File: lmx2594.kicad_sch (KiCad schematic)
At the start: 46 parts, among them J32 TUNESENSE, U21 LMX2594

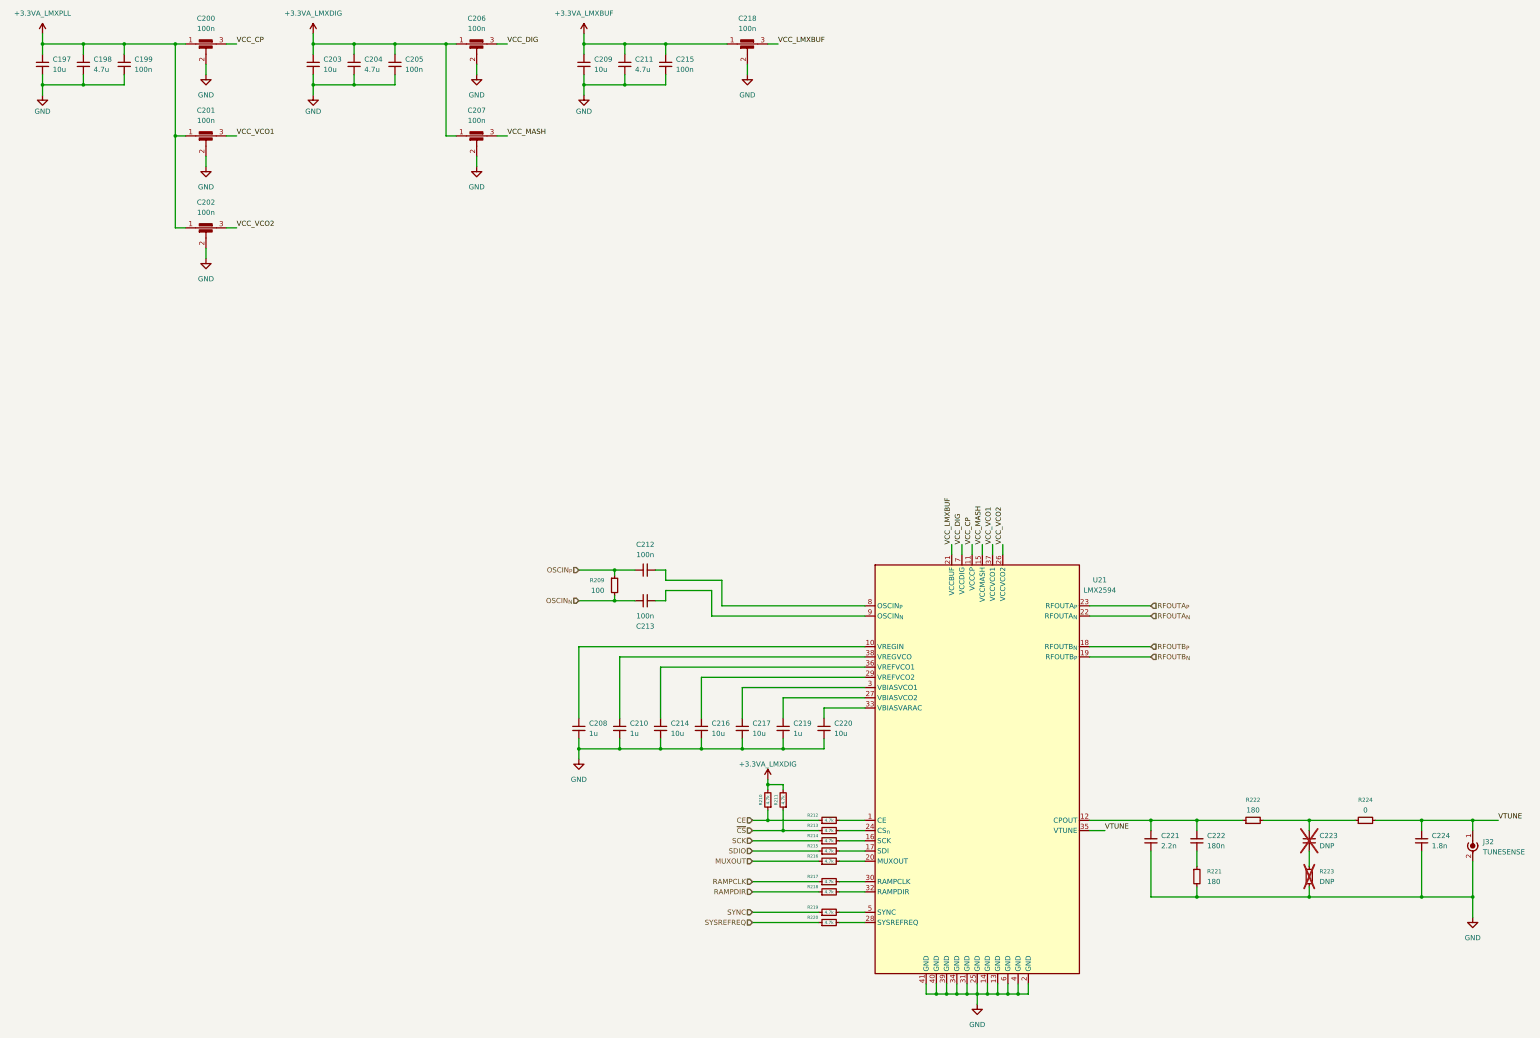
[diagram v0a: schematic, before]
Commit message: Different Matching Circuit
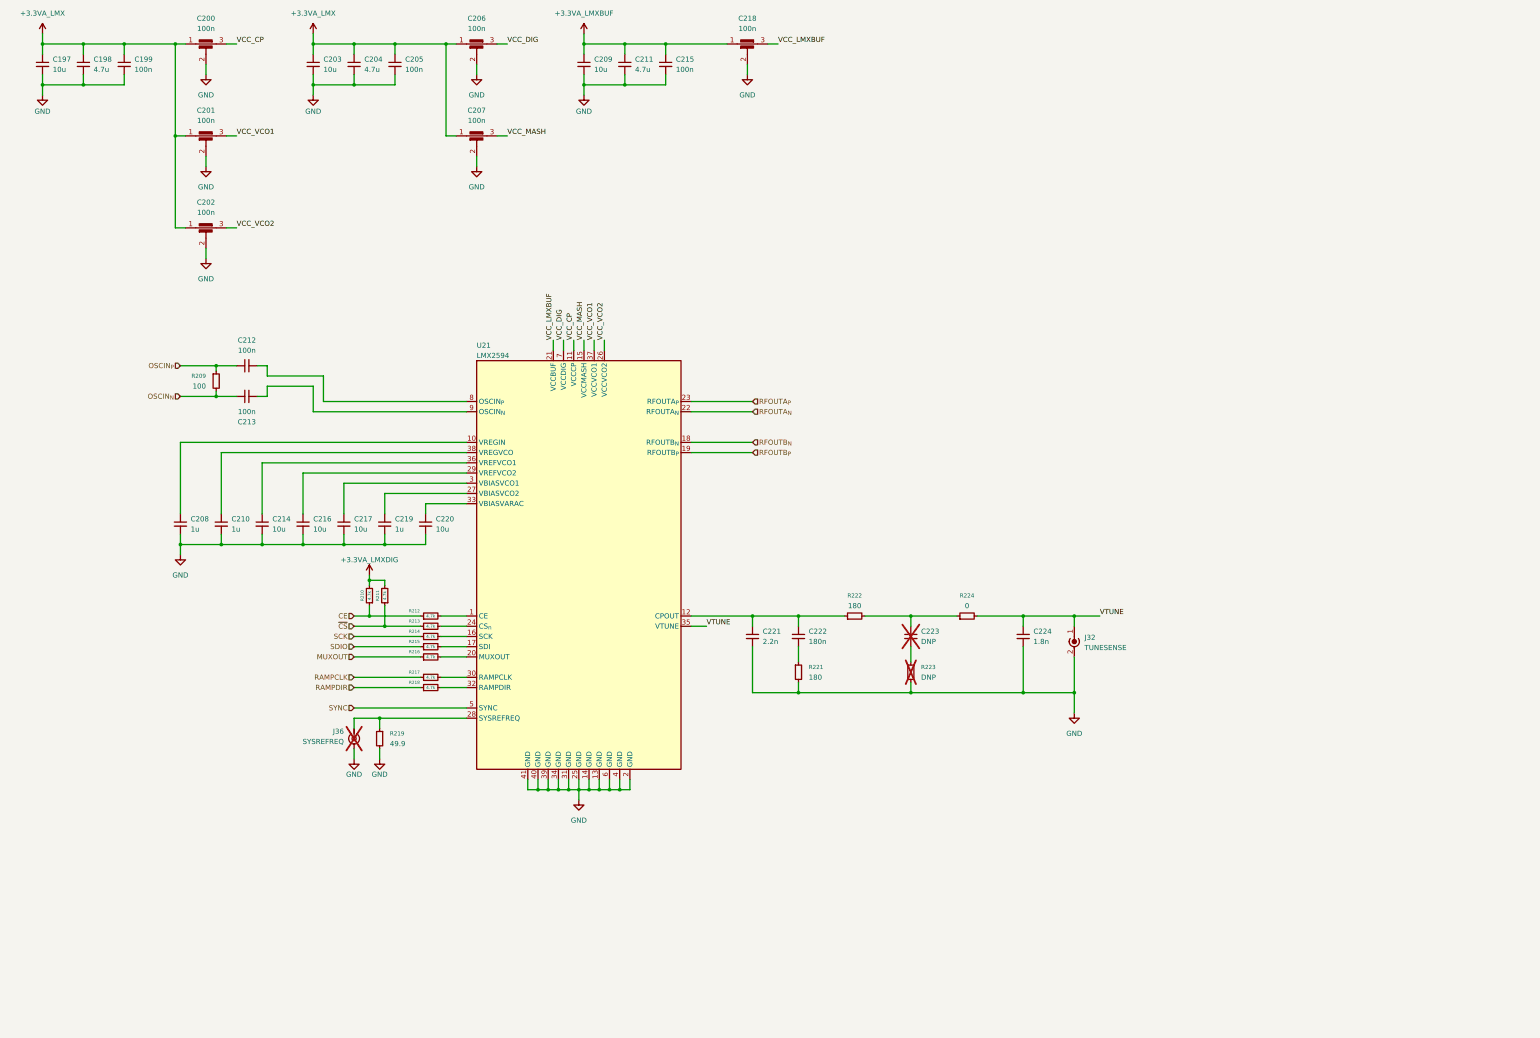
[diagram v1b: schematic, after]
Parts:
- removed R220: 4.7k, Resistor_SMD:R_0402_1005Metric, symbol Device:R_Small
- added J36: SYSREFREQ, symbol Connector:Conn_Coaxial_Small
- R219: value 4.7k -> 49.9; footprint Resistor_SMD:R_0402_1005Metric -> (none); DIGIKEY_PN 311-4.7KJRCT-ND -> (none)
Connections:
- net +3.3VA_LMXDIG: no longer C203.1, C204.1, C205.1, C206.1, C207.1
- net GND: now also R219.2, J36.2 (Ext)
- net RFOUTB_{N}: now also U21.18 (RFOUTB_{N}); no longer U21.19 (RFOUTB_{P})
- net RFOUTB_{P}: now also U21.19 (RFOUTB_{P}); no longer U21.18 (RFOUTB_{N})
- net SYNC: now also U21.5 (SYNC); no longer R219.1
- net at U21.28 (SYSREFREQ): now also R219.1, J36.1 (In)
- net +3.3VA_LMXPLL renamed +3.3VA_LMX
- net +3.3VA_LMX: now also C203.1, C204.1, C205.1, C206.1, C207.1
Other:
- moved on the sheet: C208, C210, C212, C213, C214, C216, C217, C219, C220, C221, C222, C223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
